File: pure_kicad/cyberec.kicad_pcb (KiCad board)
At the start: 4 copper layers, 50 x 50 mm, 142 parts, among them J1 XT30M, J2 XT30F, J3 XT60M, J4 XT60M, J5 Conn_01x04_Pin, J6 Conn_01x04_Pin, Q1 Q_NMOS_DGS, Q2 Q_NMOS_DGS, Q3 Q_NMOS_DGS, Q4 Q_NMOS_DGS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

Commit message: I think the routing so far is done. I've started collecting signals to route off the board
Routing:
- net /Battery Monitor/PCHG: track 1.88 -> 29.7 mm, vias 0 -> 2
- net /Battery Monitor/DSG: track 6.13 -> 32.9 mm, vias 1 -> 2
- net /Battery Monitor/CHG: track 5.58 -> 30.7 mm, vias 1 -> 2
- net -BATT: track 6.58 -> 11.6 mm, vias 5 -> 8
- net VCC: track 5.75 -> 7.19 mm, vias 1 -> 2
- net /Charger/FB: track 23.2 -> 23.8 mm

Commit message: Switch to single xt30 and JST B7B for pack, and add thermistor headers
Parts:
- removed J4: XT60M, cyberec:AMASS_XT60-M_1x02_P7.20mm_Vertical
- removed J5, J6: Conn_01x04_Pin, cyberec:JST_XH_B4B-XH-A_1x04_P2.50mm_Vertical
- added J10: Pack Thermistor 2, Connector_PinHeader_2.00mm:PinHeader_1x02_P2.00mm_Vertical, F.Cu at (95.9, 80.7)
- added J11: Pack Thermistor 1, Connector_PinHeader_2.00mm:PinHeader_1x02_P2.00mm_Vertical, F.Cu at (98.9, 80.7)
- added J12: XT30M, cyberec:AMASS_XT30U-M_1x02_P5.0mm_Vertical, F.Cu at (121.9, 83.2)
- added J7: Pack Thermistor 1, Connector_PinHeader_2.00mm:PinHeader_1x02_P2.00mm_Vertical, F.Cu at (86.9, 80.7)
- added J8: Pack Thermistor 2, Connector_PinHeader_2.00mm:PinHeader_1x02_P2.00mm_Vertical, F.Cu at (89.9, 80.7)
- added J9: Pack Thermistor 1, Connector_PinHeader_2.00mm:PinHeader_1x02_P2.00mm_Vertical, F.Cu at (92.9, 80.7)
- added NT1: NetTie_2, NetTie:NetTie-2_SMD_Pad2.0mm, B.Cu at (121.9, 81.2)
- J3: value XT60M -> Conn_01x07_Pin; footprint cyberec:AMASS_XT60-M_1x02_P7.20mm_Vertical -> cyberec:JST_XH_B7B-XH-AM_1x07_P2.50mm_Vertical
- moved J3 43.0 mm to (78.6, 93.8), turned to 90 degrees
- moved C23 5.53 mm to (82.0, 92.2)
- moved C24 5.53 mm to (82.0, 89.2)
- moved C25 5.53 mm to (82.0, 86.2)
- moved C26 5.53 mm to (82.0, 83.2)
- moved R19 5.53 mm to (82.0, 93.8)
- moved R20 5.53 mm to (82.0, 90.8)
- moved R21 5.53 mm to (82.0, 87.8)
- moved R23 5.53 mm to (82.0, 84.8)
- moved J2 5.10 mm to (121.0, 121.5), turned to 180 degrees
- moved J1 4.50 mm to (79.0, 121.5), turned to 0 degrees
- moved D10 3.55 mm to (79.8, 98.5)
- moved C27 2.66 mm to (82.0, 80.2)
- moved C28 2.66 mm to (82.0, 77.2)
- moved R24 2.66 mm to (82.0, 81.7)
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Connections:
- net /Battery Monitor/PCHG_R renamed Net-(Q5-D)
- net /Charger/VAC_DAMP renamed Net-(C45-Pad2)
- C19 pad 1: -BATT -> VSS
- C22 pad 2: -BATT -> VSS
- C28 pad 2: -BATT -> VSS
- C29 pad 1: -BATT -> VSS
- C30 pad 1: -BATT -> VSS
- C31 pad 1: -BATT -> VSS
- C32 pad 2: -BATT -> VSS
- C33 pad 2: -BATT -> VSS
- C34 pad 1: -BATT -> VSS
- J1 pad 1: VAC -> Earth
- J1 pad 2: Earth -> VAC
- J2 pad 1: VCC -> Earth
- J2 pad 2: Earth -> VCC
- J3 pad 1: +BATT -> /Battery Monitor/cell6
- J3 pad 2: /Battery Monitor/BATT_JOIN -> /Battery Monitor/cell5
- U1 pad 3: unconnected-(U1A-*INT-Pad3) -> nCHRG_INT
- U1 pad 4: unconnected-(U1A-STAT1-Pad4) -> CHRG_STAT1
- U1 pad 5: unconnected-(U1A-STAT2-Pad5) -> CHRG_STAT2
- U1 pad 6: unconnected-(U1A-*PG-Pad6) -> nCHRG_PWR_GOOD
- U2 pad 12: unconnected-(U2-TS3_ADCIN1_GPIO-Pad12) -> TS_PACK3
- U2 pad 13: unconnected-(U2-DISP_TS4_ADCIN2_GPIO_N-Pad13) -> TS_PACK4
- U2 pad 15: unconnected-(U2-DISP_GPIO_N-Pad15) -> nDISP
- U2 pad 16: unconnected-(U2-PDSG_GPIO-Pad16) -> PDSG
- U2 pad 17: unconnected-(U2-PRES_SHUTDOWN_DISP_PDSG_GPIO_N-Pad17) -> nPRES
- U2 pad 33: -BATT -> VSS
- U2 pad 9: -BATT -> VSS
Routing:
- net /Battery Monitor/BATT_JOIN: track 28.9 -> 0.00 mm
- net TS_Charge: track 4.04 -> 16.8 mm, vias 0 -> 1
- net VSS: track 0.00 -> 12.0 mm, vias 0 -> 8
- net -BATT: track 11.6 -> 0.00 mm, vias 8 -> 0
- net TS_PACK4: track 0.00 -> 8.14 mm
- net TS_PACK3: track 0.00 -> 5.64 mm
- net Net-(U2-VC6): track 14.0 -> 8.40 mm
- net TS_PACK1: track 0.00 -> 4.68 mm
- net Net-(U2-VC5): track 13.5 -> 9.25 mm
- net TS_PACK2: track 0.00 -> 3.99 mm
- net Net-(D10-K): track 10.8 -> 7.74 mm
- net /Battery Monitor/SRP: track 29.1 -> 32.1 mm
- net Net-(U2-VC4): track 11.7 -> 9.05 mm
- net /Battery Monitor/SRN: track 31.3 -> 33.7 mm
- net Net-(U2-VC2): track 14.1 -> 11.8 mm
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- added copper zone on B.Cu, net VSS
- added copper zone on In2.Cu, net VSS
- removed copper zone on In2.Cu, net -BATT
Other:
- board text added: "JSTJSTJSTJST"

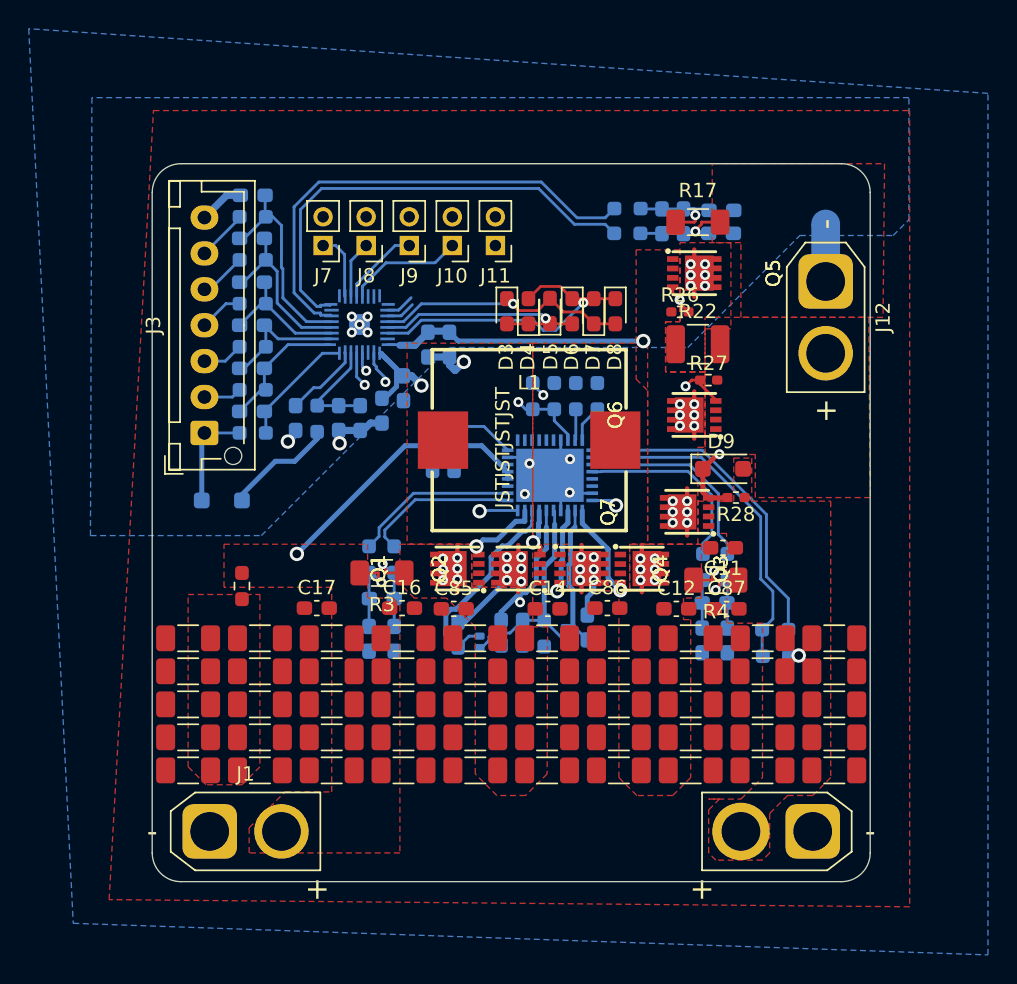
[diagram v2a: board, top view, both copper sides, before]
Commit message: Added so many pins
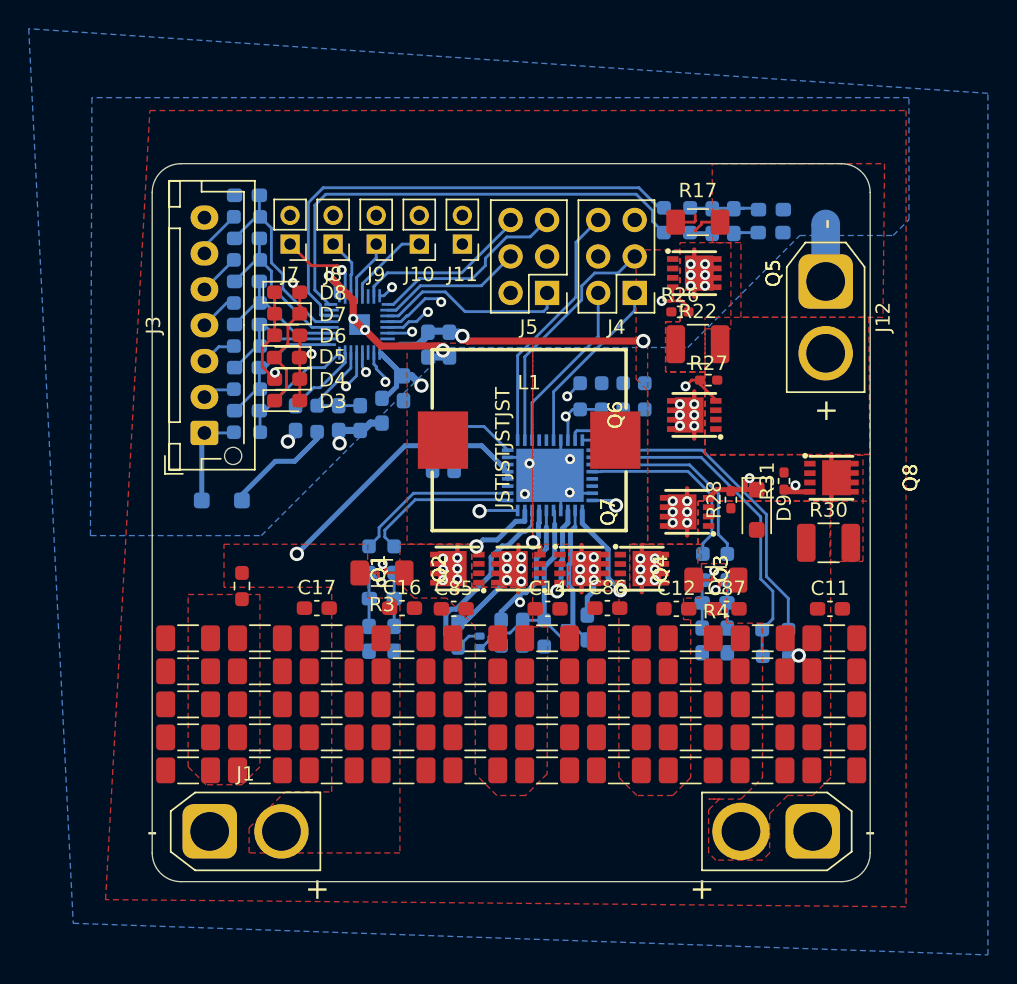
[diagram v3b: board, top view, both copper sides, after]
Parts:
- added J4: Conn_02x03_Odd_Even, Connector_PinHeader_2.54mm:PinHeader_2x03_P2.54mm_Vertical, F.Cu at (108.6, 84.0)
- added J5: Conn_02x03_Odd_Even, Connector_PinHeader_2.54mm:PinHeader_2x03_P2.54mm_Vertical, F.Cu at (102.5, 84.0)
- added Q8: Q_NMOS_DGS, cyberec:DFN-8_L3.0-W3.0-P0.65-BL-4, F.Cu at (122.3, 96.9)
- added R30: 1k, 500mW, cyberec:R_1210_3225Metric_Pad1.30x2.65mm_HandSolder, F.Cu at (122.1, 101.4)
- added R31: 10M, cyberec:R_0402_1005Metric_Pad0.72x0.64mm_HandSolder, F.Cu at (119.0, 97.1)
- moved D8 22.9 mm to (84.4, 84.0), turned to 0 degrees
- moved D7 21.4 mm to (84.4, 85.5), turned to 180 degrees
- moved D6 19.9 mm to (84.4, 87.0), turned to 0 degrees
- moved D5 18.6 mm to (84.4, 88.5), turned to 180 degrees
- moved D4 17.5 mm to (84.4, 90.0), turned to 180 degrees
- moved D3 16.5 mm to (84.4, 91.5), turned to 0 degrees
- moved C11 8.58 mm to (122.2, 106.0), turned to 0 degrees
- moved D9 3.69 mm to (117.1, 99.1), turned to -90 degrees
- moved C20 3.50 mm to (115.5, 79.0)
- moved C21 3.50 mm to (114.0, 79.0)
- moved C19 3.45 mm to (118.1, 79.8)
- moved C22 3.45 mm to (118.1, 78.2)
- moved R18 3.45 mm to (111.5, 78.1)
- moved R16 3.45 mm to (111.5, 79.8)
- moved R10 3.30 mm to (106.3, 91.2)
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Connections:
- net Net-(Q5-D) renamed /Battery Monitor/PCHG_R
- U2 pad 16: PDSG -> /Battery Monitor/PDSG
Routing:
- net /Battery Monitor/PDSG: track 0.00 -> 41.2 mm, vias 0 -> 2
- net SCL: track 0.00 -> 17.7 mm
- net SDA: track 0.00 -> 16.9 mm
- net nPRES: track 0.00 -> 13.8 mm
- net nCHRG_PWR_GOOD: track 0.00 -> 12.6 mm
- net nDISP: track 0.00 -> 12.3 mm
- net nCHRG_INT: track 0.00 -> 12.2 mm
- net SMBC: track 2.05 -> 13.5 mm
- net SMBD: track 2.00 -> 10.1 mm
- net VSS: track 12.0 -> 20.0 mm, vias 8 -> 6
- net /Battery Monitor/LED_A: track 18.2 -> 25.2 mm, vias 1 -> 2
- net TS_Charge: track 16.8 -> 21.0 mm
- net /Battery Monitor/LED_B: track 16.0 -> 18.7 mm, vias 1 -> 2
- net Net-(U1A-ILIM_HIZ): track 2.59 -> 5.24 mm
- net /Battery Monitor/LED_C: track 21.8 -> 19.2 mm, vias 1 -> 2
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- added copper zone on F.Cu, net /Battery Monitor/PDSG_R

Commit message: Move IO to bottom edge, clean up routing, labels
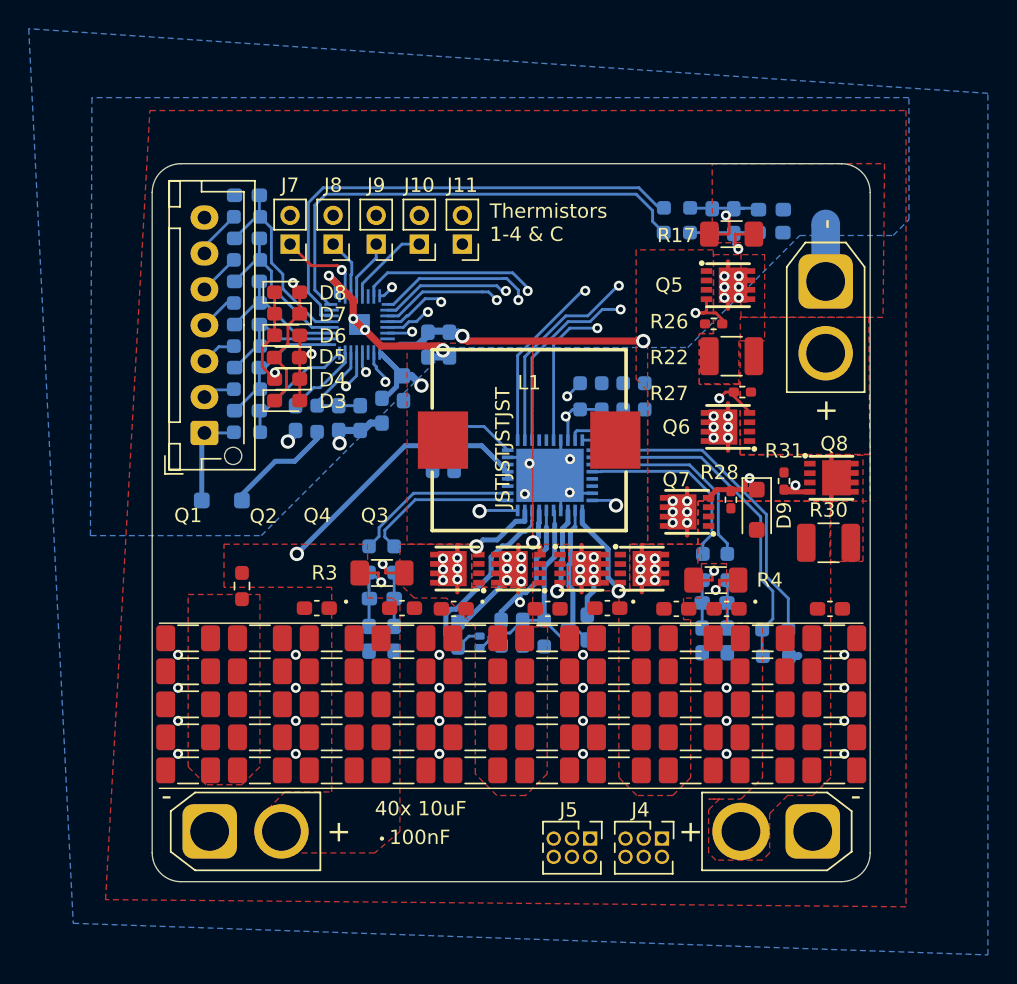
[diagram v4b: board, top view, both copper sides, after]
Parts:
- J4, J5: footprint Connector_PinHeader_2.54mm:PinHeader_2x03_P2.54mm_Vertical -> Connector_PinHeader_1.27mm:PinHeader_2x03_P1.27mm_Vertical
- moved J5 38.1 mm to (105.5, 122.0), turned to -90 degrees
- moved J4 38.0 mm to (110.5, 122.0), turned to -90 degrees
- moved R17 2.49 mm to (115.3, 79.9)
- moved R22 2.49 mm to (115.3, 88.4)
- moved R26 2.49 mm to (114.1, 86.2)
- moved R27 2.49 mm to (116.1, 90.9)
- moved Q5 2.49 mm to (115.1, 83.5)
- moved Q6 2.49 mm to (115.1, 93.3)
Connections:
- J5 pad 1: SMBC -> nPRES
- J5 pad 2: Earth -> nDISP
- J5 pad 4: SMBD -> SMBC
- J5 pad 5: nPRES -> SMBD
- J5 pad 6: nDISP -> Earth
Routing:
- net nDISP: track 12.3 -> 69.9 mm, vias 0 -> 1
- net SMBD: track 10.1 -> 61.6 mm, vias 0 -> 1
- net nPRES: track 13.8 -> 64.9 mm, vias 0 -> 1
- net SMBC: track 13.5 -> 63.2 mm, vias 0 -> 1
- net nCHRG_INT: track 12.2 -> 60.9 mm, vias 0 -> 1
- net SDA: track 16.9 -> 62.7 mm, vias 0 -> 1
- net SCL: track 17.7 -> 61.9 mm, vias 0 -> 1
- net nCHRG_PWR_GOOD: track 12.6 -> 54.3 mm, vias 0 -> 1
- net /Battery Monitor/CHG: track 30.5 -> 33.2 mm
- net Net-(C20-Pad2): track 6.09 -> 7.73 mm, vias 0 -> 1
- net Net-(C19-Pad2): track 6.16 -> 7.68 mm, vias 0 -> 1
- net TS_Charge: track 21.0 -> 22.5 mm
- net /Battery Monitor/PCHG: track 28.8 -> 30.2 mm
- net /Battery Monitor/PDSG: track 41.2 -> 42.1 mm
- net VCC: vias 2 -> 1
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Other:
- board text added: "100nF"
- board text added: "40x 10uF"
- board text added: "CyberBMS Stefan Buller 2025-07-30"
- board text added: "Thermistors 1-4 & C"
